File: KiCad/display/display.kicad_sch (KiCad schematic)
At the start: 8 parts, among them J4 Conn_01x05_Pin, U3 Display

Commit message: schematics finished
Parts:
- R1, R2: value 2k -> 2k2; now not fitted

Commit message: PCB designs started
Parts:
- renumbered J4 to J1, R4 to R1, R3 to R2, R2 to R3, R1 to R4, U3 to U1
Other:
- note added: "A0 low (JP1 open) : addr = 0b0111100 A0 high (JP1 closed): addr = 0b0111101"
- note removed: "A0 low (JP0 open) : addr = 0b0111100 A0 high (JP0 closed): addr = 0b0111101"
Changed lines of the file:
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@@
 		)
 	)
-	(text "A0 low (JP0 open)   : addr = 0b0111100\nA0 high (JP0 closed): addr = 0b0111101\n"
+	(text "A0 low (JP1 open)   : addr = 0b0111100\nA0 high (JP1 closed): addr = 0b0111101\n"
 		(exclude_from_sim no)
 		(at 110.49 19.05 0)
@@
 		(dnp no)
 		(fields_autoplaced yes)
-		(property "Reference" "#PWR04"
+		(property "Reference" "#PWR03"
 			(at 133.35 82.55 0)
 			(effects
@@
 			(project "KITTEN"
 				(path "/c14c77e6-5108-4122-81fc-9f298705addb"
-					(reference "#PWR04")
+					(reference "#PWR03")
 					(unit 1)
 				)
@@
 		(dnp no)
 		(fields_autoplaced yes)
-		(property "Reference" "#PWR010"
+		(property "Reference" "#PWR06"
 			(at 185.42 109.22 0)
 			(effects
@@
 			(project "KITTEN"
 				(path "/c14c77e6-5108-4122-81fc-9f298705addb"
-					(reference "#PWR010")
+					(reference "#PWR06")
 					(unit 1)
 				)
@@
 		(on_board yes)
 		(dnp no)
-		(property "Reference" "U3"
+		(property "Reference" "U1"
 			(at 50.8 61.722 0)
 			(effects
@@
 			(project ""
 				(path "/c14c77e6-5108-4122-81fc-9f298705addb"
-					(reference "U3")
+					(reference "U1")
 					(unit 1)
 				)
@@
 		(dnp no)
 		(fields_autoplaced yes)
-		(property "Reference" "#PWR06"
+		(property "Reference" "#PWR09"
 			(at 238.76 87.63 0)
 			(effects
@@
 			(project "KITTEN"
 				(path "/c14c77e6-5108-4122-81fc-9f298705addb"
-					(reference "#PWR06")
+					(reference "#PWR09")
 					(unit 1)
 				)
@@
 		(dnp yes)
 		(fields_autoplaced yes)
-		(property "Reference" "R2"
+		(property "Reference" "R3"
 			(at 241.3 88.8999 0)
 			(effects
@@
 			(project "KITTEN"
 				(path "/c14c77e6-5108-4122-81fc-9f298705addb"
-					(reference "R2")
+					(reference "R3")
 					(unit 1)
 				)
@@
 		(dnp no)
 		(fields_autoplaced yes)
-		(property "Reference" "R4"
+		(property "Reference" "R1"
 			(at 135.89 95.2499 0)
 			(effects
@@
 			(project "KITTEN"
 				(path "/c14c77e6-5108-4122-81fc-9f298705addb"
-					(reference "R4")
+					(reference "R1")
 					(unit 1)
 				)
@@
 		(on_board yes)
 		(dnp no)
-		(property "Reference" "J4"
+		(property "Reference" "J1"
 			(at 267.335 88.9 0)
 			(effects
@@
 			(project ""
 				(path "/c14c77e6-5108-4122-81fc-9f298705addb"
-					(reference "J4")
+					(reference "J1")
 					(unit 1)
 				)
@@
 		(dnp no)
 		(fields_autoplaced yes)
-		(property "Reference" "#PWR03"
+		(property "Reference" "#PWR04"
 			(at 133.35 109.22 0)
 			(effects
@@
 			(project "KITTEN"
 				(path "/c14c77e6-5108-4122-81fc-9f298705addb"
-					(reference "#PWR03")
+					(reference "#PWR04")
 					(unit 1)
 				)
@@
 		(dnp no)
 		(fields_autoplaced yes)
-		(property "Reference" "#PWR09"
+		(property "Reference" "#PWR05"
 			(at 185.42 83.82 0)
 			(effects
@@
 			(project "KITTEN"
 				(path "/c14c77e6-5108-4122-81fc-9f298705addb"
-					(reference "#PWR09")
+					(reference "#PWR05")
 					(unit 1)
 				)
@@
 		(dnp no)
 		(fields_autoplaced yes)
-		(property "Reference" "R3"
+		(property "Reference" "R2"
 			(at 187.96 85.0899 0)
 			(effects
@@
 			(project "KITTEN"
 				(path "/c14c77e6-5108-4122-81fc-9f298705addb"
-					(reference "R3")
+					(reference "R2")
 					(unit 1)
 				)
@@
 		(dnp no)
 		(fields_autoplaced yes)
-		(property "Reference" "#PWR05"
+		(property "Reference" "#PWR010"
 			(at 255.27 85.09 0)
 			(effects
@@
 			(project "KITTEN"
 				(path "/c14c77e6-5108-4122-81fc-9f298705addb"
-					(reference "#PWR05")
+					(reference "#PWR010")
 					(unit 1)
 				)
@@
 		(dnp yes)
 		(fields_autoplaced yes)
-		(property "Reference" "R1"
+		(property "Reference" "R4"
 			(at 257.81 86.3599 0)
 			(effects
@@
 			(project ""
 				(path "/c14c77e6-5108-4122-81fc-9f298705addb"
-					(reference "R1")
+					(reference "R4")
 					(unit 1)
 				)

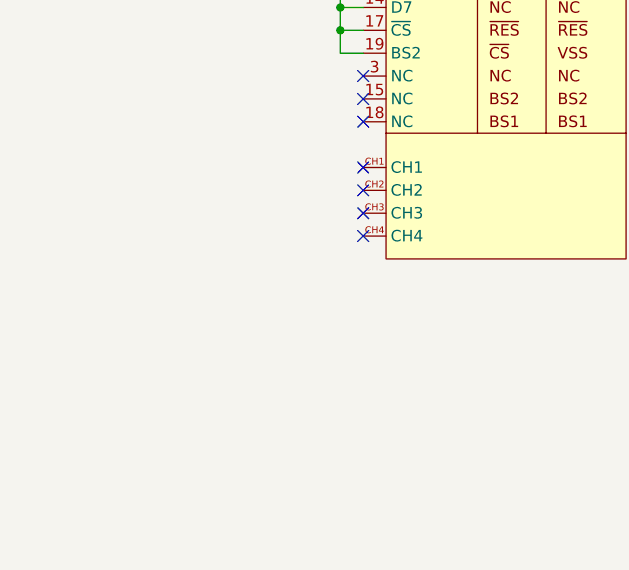
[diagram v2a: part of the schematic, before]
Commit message: PCB bugfixes based on review
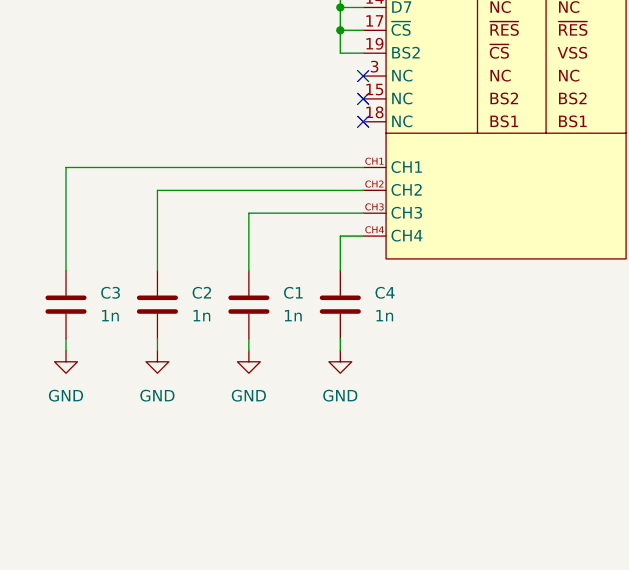
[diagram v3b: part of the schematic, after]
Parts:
- added C1, C2, C3, C4: 1n, Capacitor_SMD:C_0603_1608Metric, symbol Device:C
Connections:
- net GND: now also C1.2, C2.2, C3.2, C4.2
- net at U1.CH1: now also C3.1
- net at U1.CH2: now also C2.1
- net at U1.CH3: now also C1.1
- net at U1.CH4: now also C4.1
- no-connect marks 7 -> 3

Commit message: exports
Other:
- title: (none) -> OLED modul
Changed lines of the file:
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@@
 	(generator_version "9.0")
 	(paper "A4")
+	(title_block
+		(title "OLED modul")
+	)
 	(rectangle
 		(start 210.8201 12.319)
